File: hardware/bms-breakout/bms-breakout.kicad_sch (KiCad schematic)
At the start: 32 parts, among them J1 IN-A, J10 V-SUPP, J11 Smol_Brain_Board, J13 UART_CONN, J16 ESTOP_CON, J17 I2C_Conn, J18 BAL_3, J19 BAL_2, J2 IN-B, J20 BAL_1, J21 DE9_Socket_MountingHoles, J22 DE9_Socket_MountingHoles, J23 FAN-IN, J24 SWITCH, J3 IN-C, J4 BALANCE-A, J5 BALANCE-B, J6 BALANCE-C, J7 Conn_01x02, Q1 PMOZZ, SW1 Kill_Switch

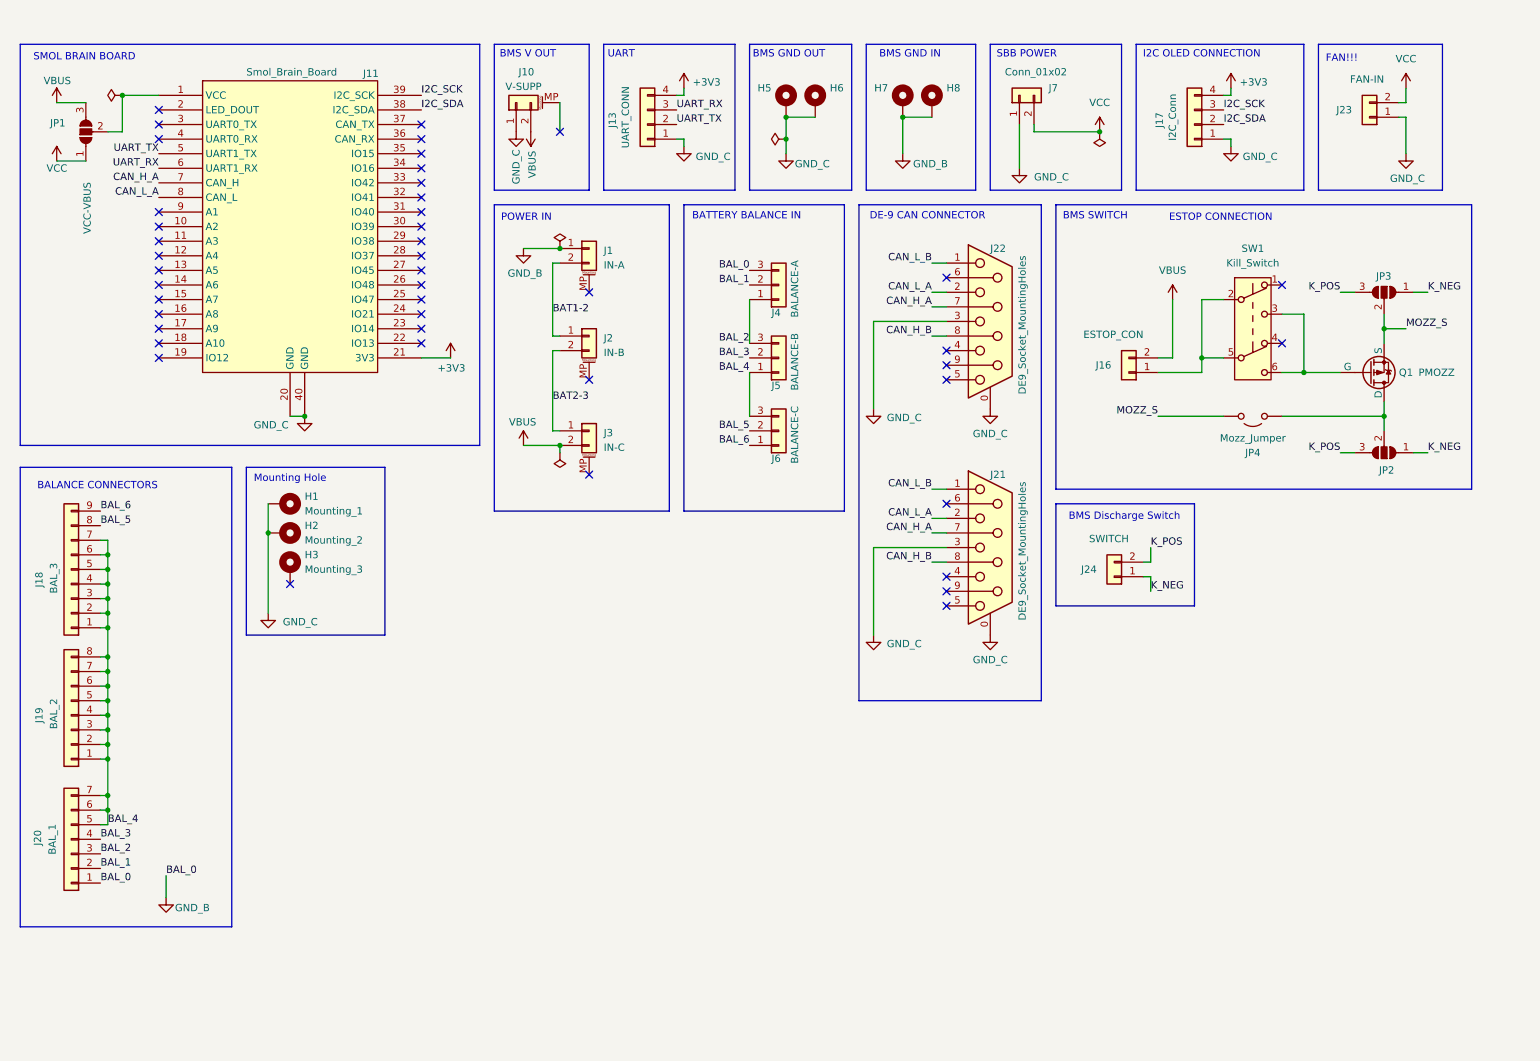
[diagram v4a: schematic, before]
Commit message: Final Touches
- Added graphics
- Added text
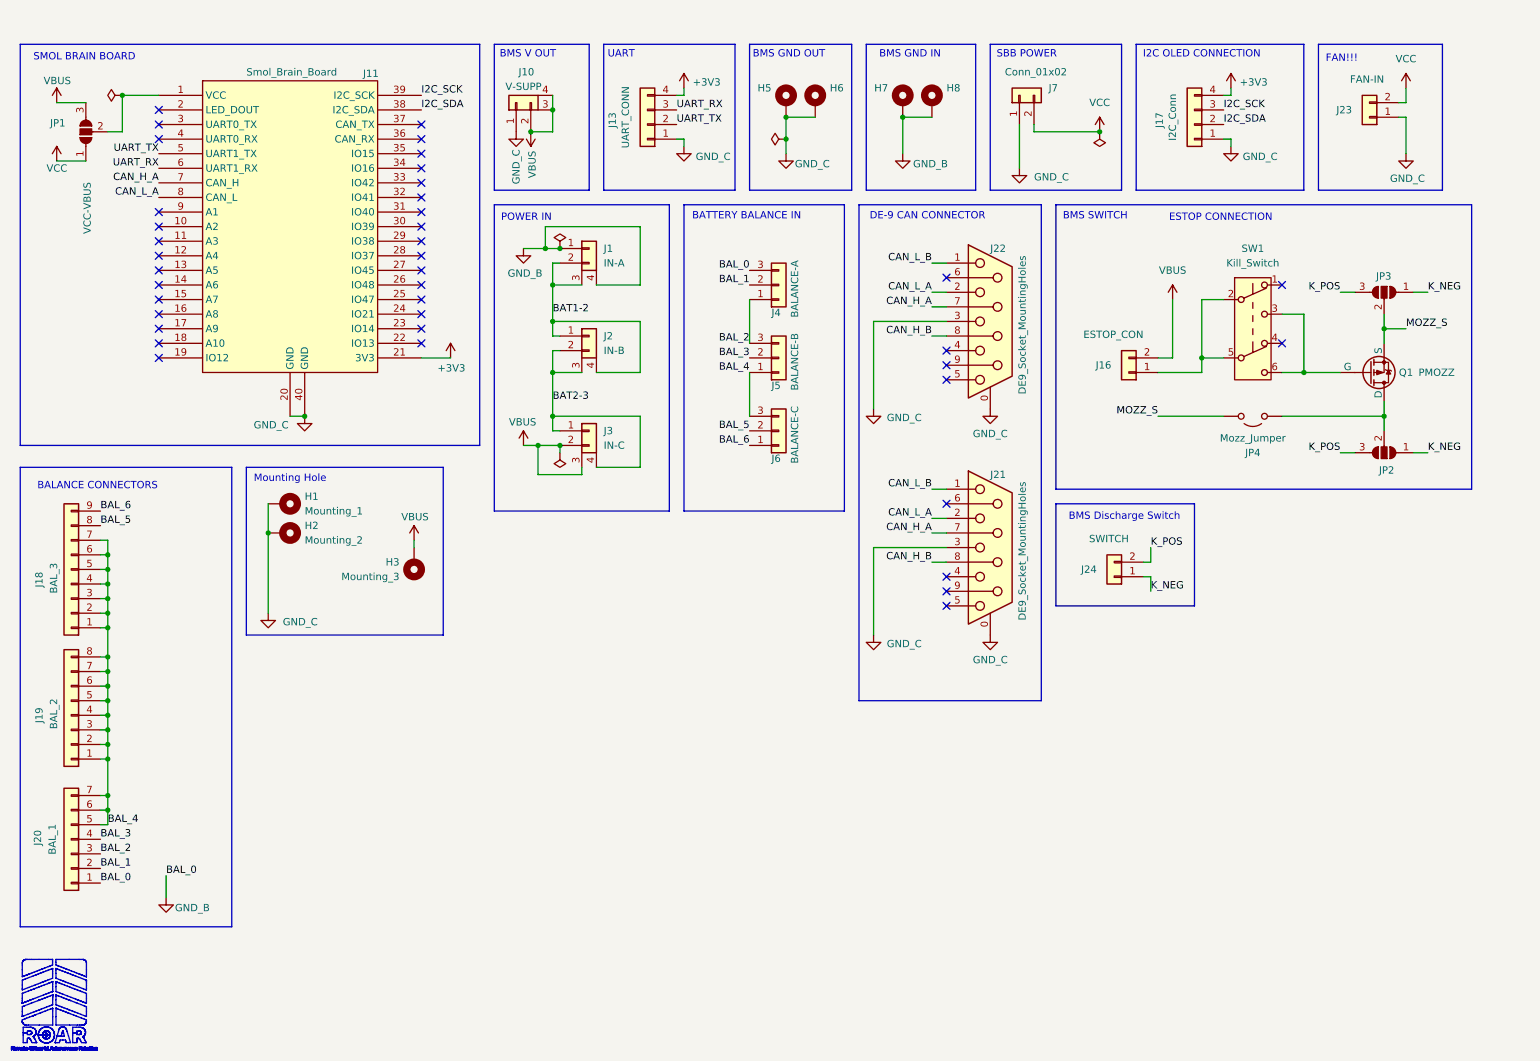
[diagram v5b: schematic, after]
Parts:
- J1: footprint Connector_AMASS:AMASS_XT90PW-M_1x02_P10.90mm_Horizontal -> custom-XT90:AMASS_XT90PW-M_1x02_P10.90mm_Horizontal; symbol Connector_Generic_MountingPin:Conn_01x02_MountingPin -> Connector_Generic:Conn_01x02
- J10, J2, J3: footprint Connector_AMASS:AMASS_XT90PW-M_1x02_P10.90mm_Horizontal -> custom-XT90:AMASS_XT90PW-M_1x02_P10.90mm_Horizontal; symbol Connector_Generic_MountingPin:Conn_01x02_MountingPin -> custom_power:Conn_01x02_2_Mounting_Points
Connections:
- net BAT1-2: now also J1.3 (M1), J2.4 (M1)
- net BAT2-3: now also J2.3 (M1), J3.4 (M1)
- net GND_B: now also J1.4 (M1)
- net VBUS: now also H3.1, J10.3 (M1), J10.4 (M1), J3.3 (M1)
- no-connect marks 45 -> 40
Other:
- moved on the sheet: H3, J1, J10, J2, J3

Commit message: Finished, ready for review
- Cleaned up traces
- Repositioned sw output
- Added edges
- Other finishes
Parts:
- JP4: footprint Jumper:SolderJumper-2_P1.3mm_Open_RoundedPad1.0x1.5mm -> Jumper:SolderJumper-2_P1.3mm_Bridged_RoundedPad1.0x1.5mm; symbol Jumper:Jumper_2_Open -> Jumper:Jumper_2_Bridged
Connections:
- net at JP2.2 (C), JP4.2 (B): no longer Q1.1 (D)
- net MOZZ_S: no longer names the net of JP3.2 (C), Q1.3 (S)
- net MOZZ_S: no longer JP4.1 (A)
- new net MOZZ_D: JP4.1 (A), Q1.1 (D)
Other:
- note added: "When K_POS and K_NEG are connected the BMS discharges its mozfets and switches off. The jumper is if the mozfet does not work. The killswitch needs to be switched on for the batteries to run."
- moved on the sheet: J24, JP2, JP4

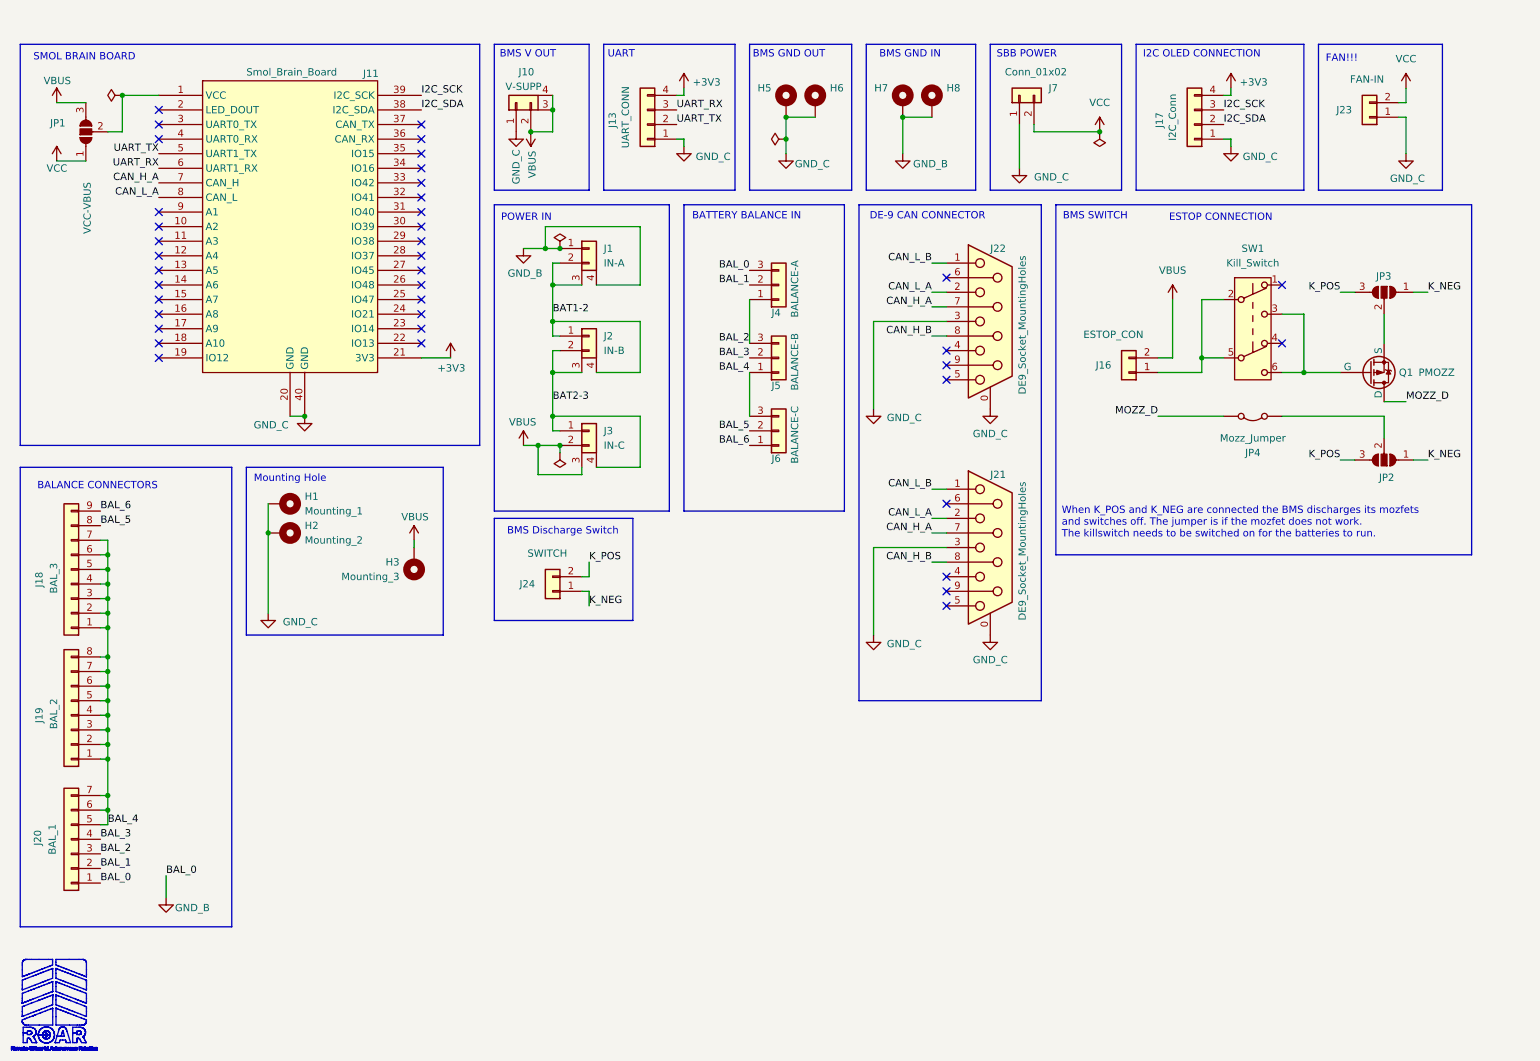
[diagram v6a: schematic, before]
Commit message: Redesigned switch off method
- Added NType MosFet for PWM for Fan
- Added voltage divider / pulldown resistor for mosfet control
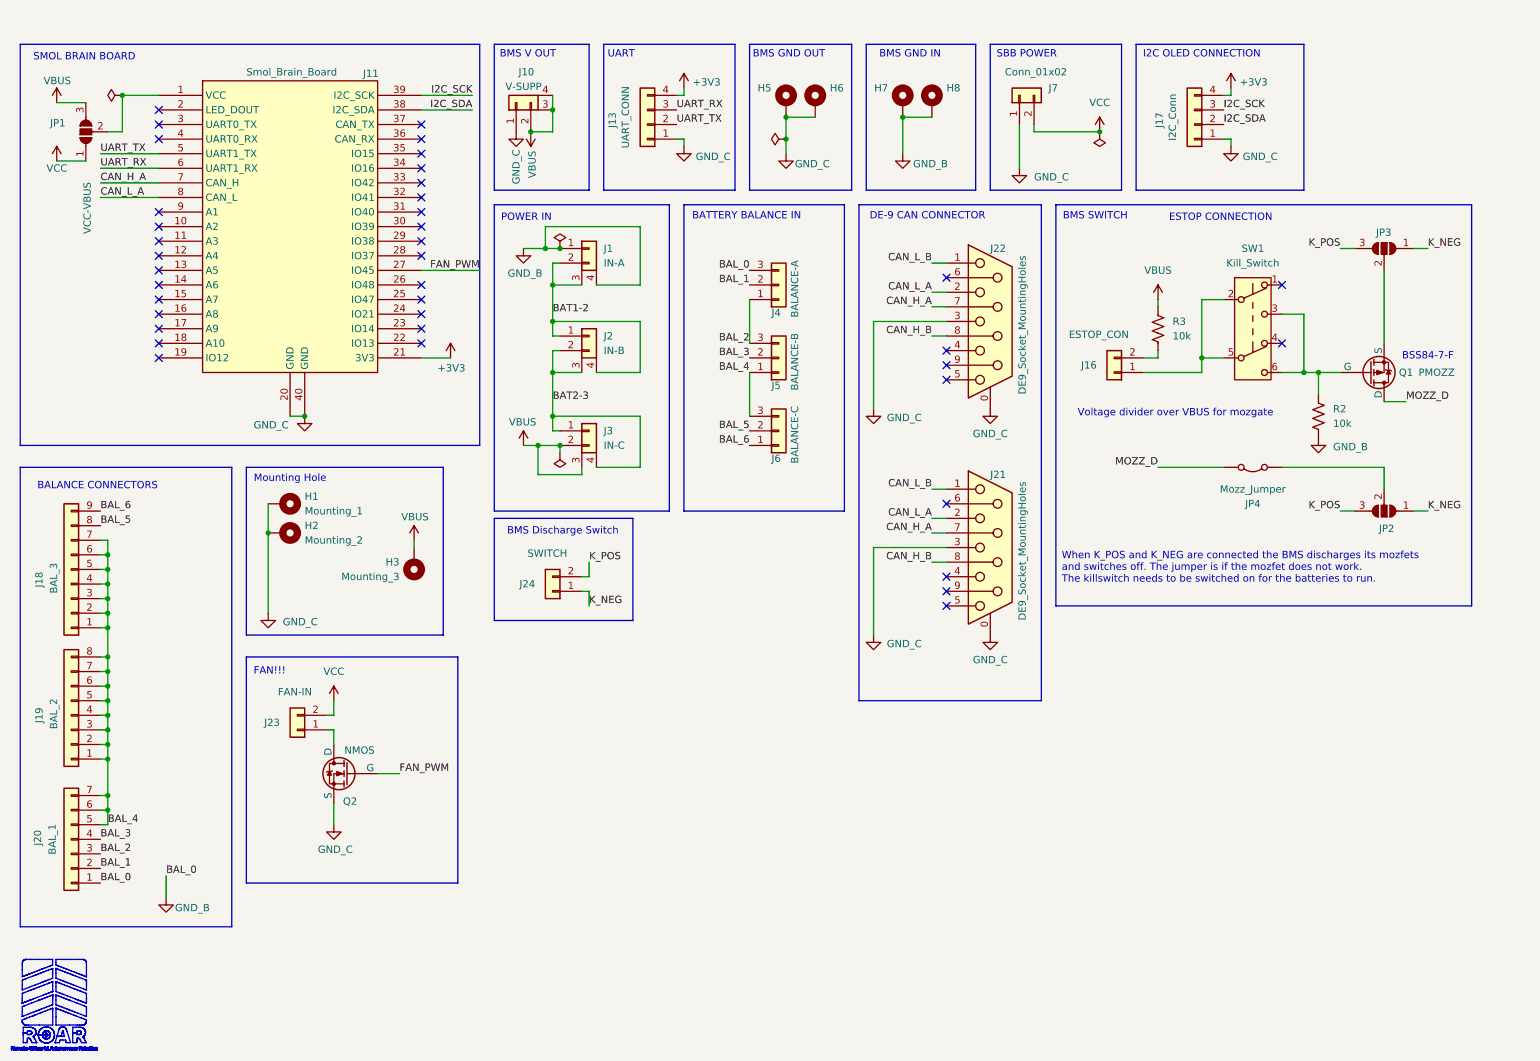
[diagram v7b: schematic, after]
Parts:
- added Q2: NMOS, Package_TO_SOT_SMD:SOT-23-3, symbol Simulation_SPICE:NMOS
- added R2, R3: 10k, Resistor_SMD:R_0805_2012Metric_Pad1.20x1.40mm_HandSolder, symbol Device:R_US
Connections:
- net GND_B: now also R2.2
- net GND_C: now also Q2.3 (S); no longer J23.1 (Pin_1)
- net VBUS: now also R3.1; no longer J16.2 (Pin_2)
- net at Q1.2 (G), SW1.3 (C), SW1.6 (C): now also R2.1
- net FAN_PWM: now reaches J11.27 (IO45)
- net FAN_PWM: now also Q2.2 (G)
- new net: J23.1 (Pin_1), Q2.1 (D)
- new net: J16.2 (Pin_2), R3.2
- no-connect marks 40 -> 39
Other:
- note added: "BSS84-7-F"
- note added: "Voltage divider over VBUS for mozgate"
- moved on the sheet: J16, J23, JP2, JP3, JP4

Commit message: Changed footprint for switch
- Changed footprint for switch
- Edited traces accordingly
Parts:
- SW1: footprint Button_Switch_THT:SW_CK_JS202011CQN_DPDT_Straight -> Button_Switch_THT:SW_Tactile_Straight_KSA0Axx1LFTR
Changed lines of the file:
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@@
 			)
 		)
-		(property "Footprint" "Button_Switch_THT:SW_CK_JS202011CQN_DPDT_Straight"
+		(property "Footprint" "Button_Switch_THT:SW_Tactile_Straight_KSA0Axx1LFTR"
 			(at 234.95 62.23 0)
 			(effects
